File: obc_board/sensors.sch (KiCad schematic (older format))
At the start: 74 parts

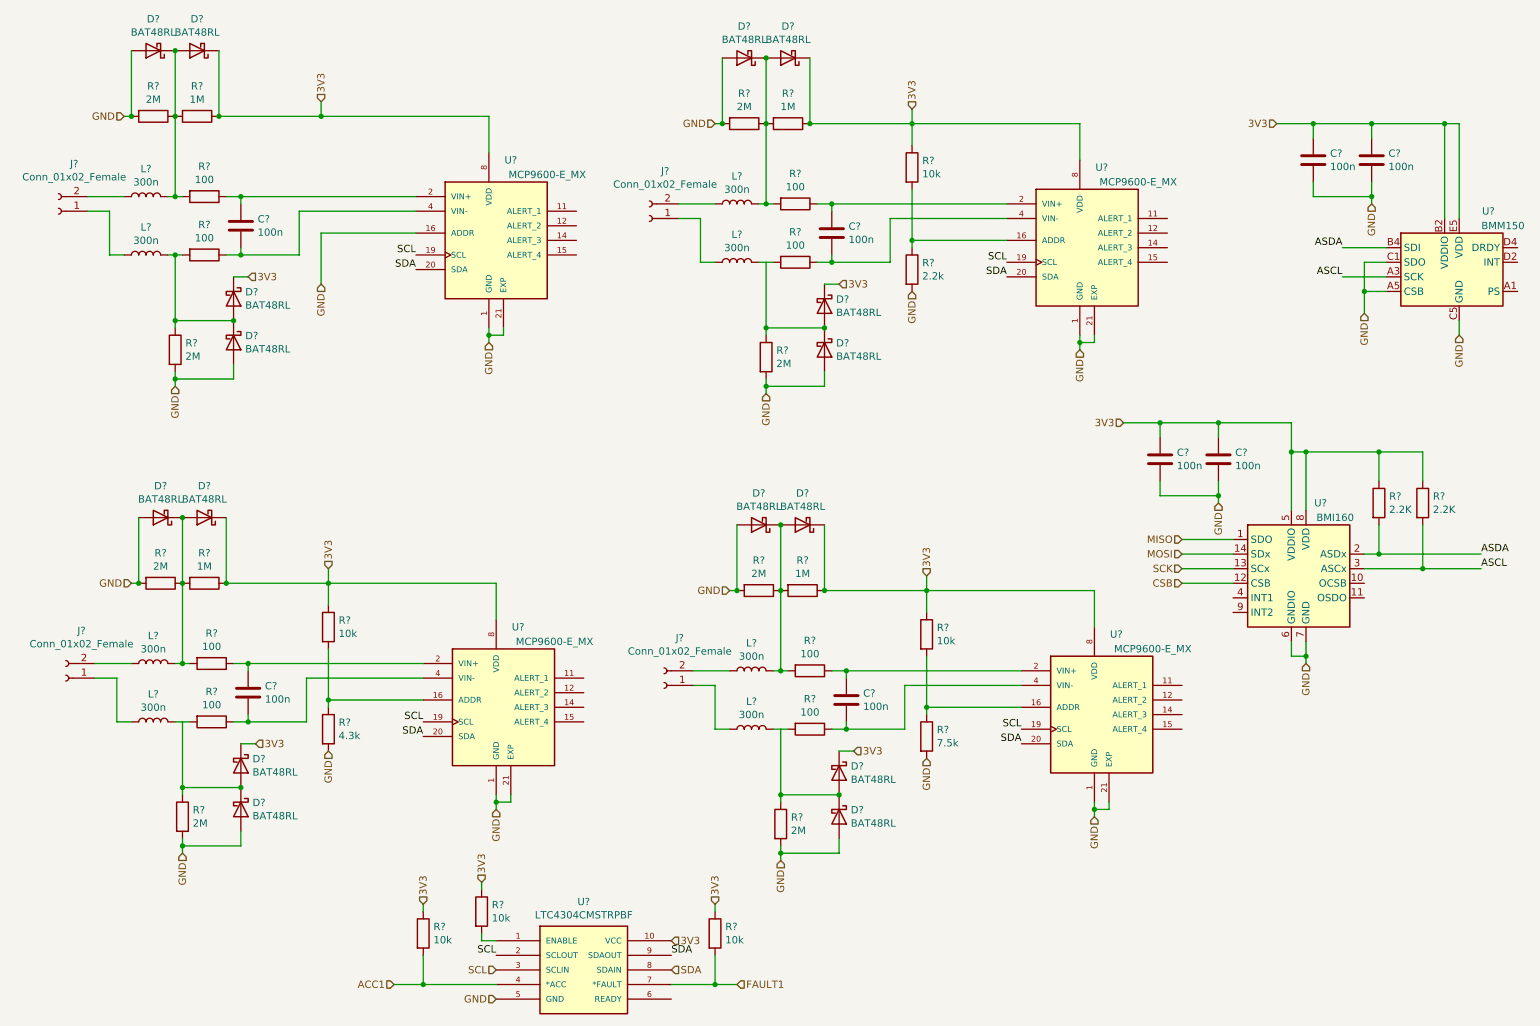
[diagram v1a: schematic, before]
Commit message: updated footprints
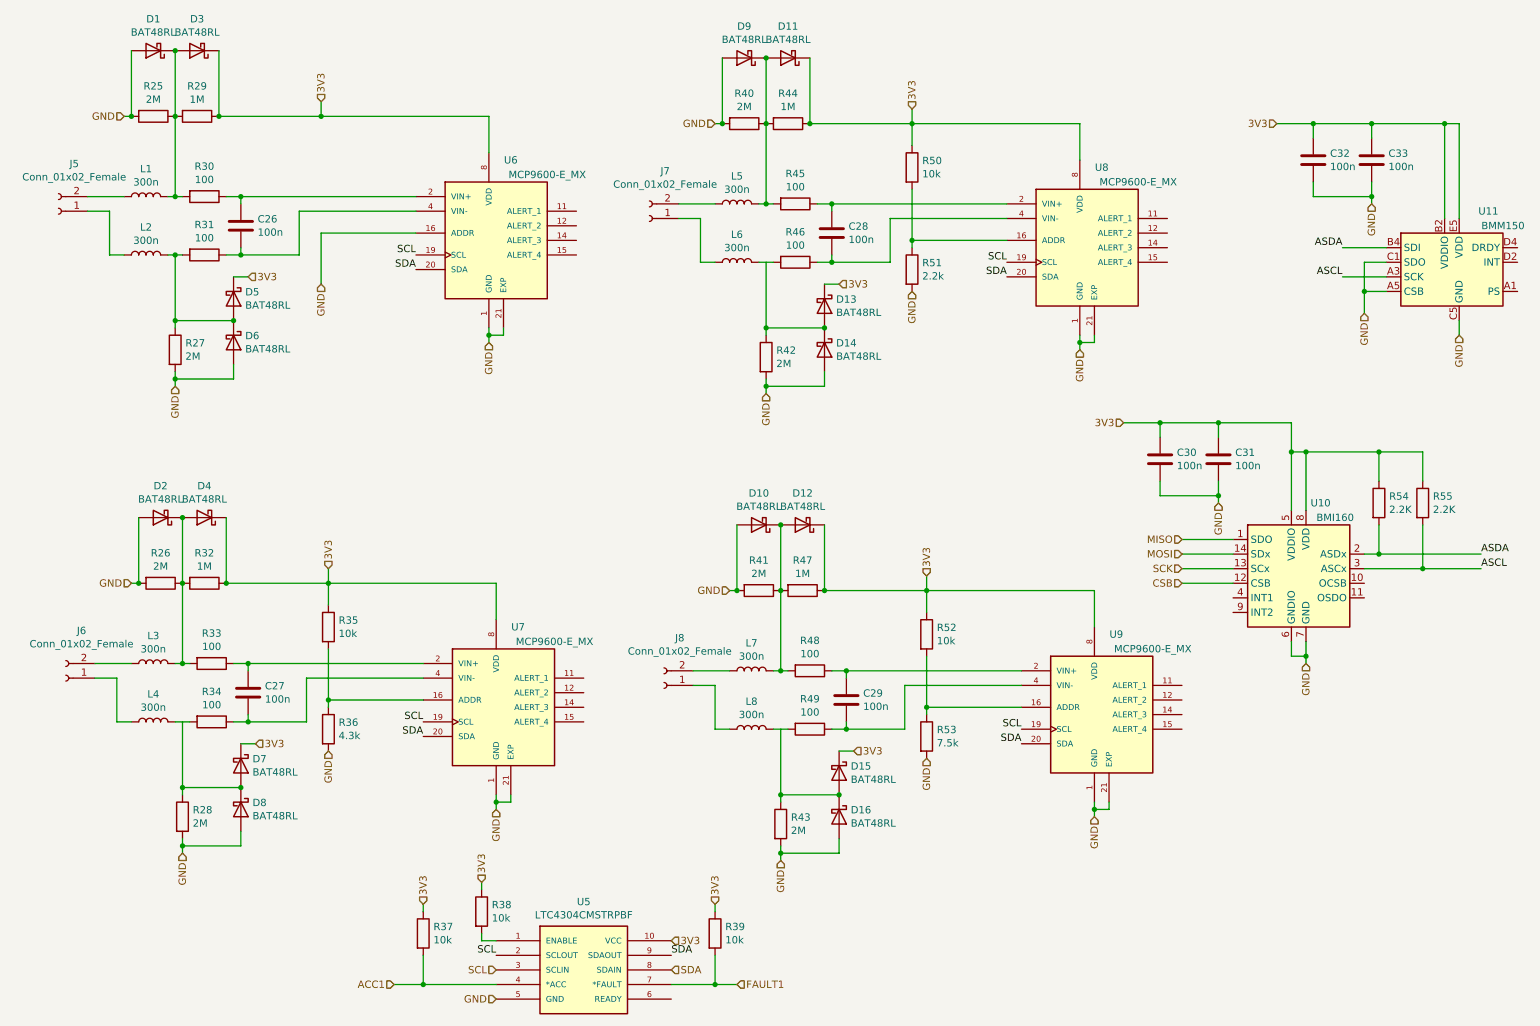
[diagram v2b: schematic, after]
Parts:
- C26, C27, C28, C29, C30, C31, C32, C33: renamed from C?; footprint (none) -> cubesat_obc:CAPC1005X55N; Digikey Part Number (none) -> 490-13342-1-ND
- U10: renamed from U?; Digikey Part Number (none) -> 828-1057-1-ND
- U11: renamed from U?; Digikey Part Number (none) -> 828-1044-1-ND
- U5: renamed from U?; footprint MSOP-10_MS -> Package_SO:MSOP-10_3x3mm_P0.5mm; Digikey Part Number (none) -> LTC4304CMS#PBF-ND
- U6, U7, U8, U9: renamed from U?; footprint QFN65P500X500X100-21N_MCP9600-E/MX -> Package_DFN_QFN:QFN-20-1EP_5x5mm_P0.65mm_EP3.35x3.35mm_ThermalVias; Digikey Part Number (none) -> MCP9600-E/MX-ND
- gave numbers to parts that had none: 59

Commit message: footprints
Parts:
- C26, C27, C28, C29, C30, C31, C32, C33: footprint cubesat_obc:CAPC1005X55N -> Capacitor_SMD:C_0402_1005Metric; Digikey Part Number 490-13342-1-ND -> 490-16433-1-ND
- D1, D10, D11, D12, D13, D14, D15, D16, D2, D3, D4, D5, D6, D7, D8, D9: footprint Diode_THT:D_DO-35_SOD27_P7.62mm_Horizontal -> Diode_SMD:D_MiniMELF; Digikey Part Number (none) -> 497-3274-1-ND
- J5, J6, J7, J8: footprint (none) -> Connector_Molex:Molex_PicoBlade_53398-0271_1x02-1MP_P1.25mm_Vertical; Digikey Part Number (none) -> WM7606CT-ND
- L1, L2, L3, L4, L5, L6, L7, L8: footprint (none) -> Inductor_SMD:L_1210_3225Metric; Digikey Part Number (none) -> 732-7338-2-ND
- R25, R26, R27, R28, R40, R41, R42, R43: footprint (none) -> Resistor_SMD:R_0603_1608Metric; Digikey Part Number (none) -> 311-2.00MHRCT-ND
- R29, R32, R44, R47: footprint (none) -> Resistor_SMD:R_0603_1608Metric; Digikey Part Number (none) -> 11-1.00MHRCT-ND
- R30, R31, R33, R34, R45, R46, R48, R49: footprint (none) -> Resistor_SMD:R_0402_1005Metric; Digikey Part Number (none) -> 311-100LRCT-ND
- R35, R37, R38, R39, R50, R52: footprint (none) -> Resistor_SMD:R_0402_1005Metric; Digikey Part Number (none) -> 311-10.0KLRCT-ND
- R36: footprint (none) -> Resistor_SMD:R_0402_1005Metric; Digikey Part Number (none) -> 311-4.30KLRCT-ND
- R51: footprint (none) -> Resistor_SMD:R_0402_1005Metric; Digikey Part Number (none) -> 311-2.20KLRCT-ND
- R53: footprint (none) -> Resistor_SMD:R_0402_1005Metric; Digikey Part Number (none) -> 311-7.50KLRCT-ND
- R54, R55: value 2.2K -> 2.2k; footprint (none) -> Resistor_SMD:R_0402_1005Metric; Digikey Part Number (none) -> 311-2.20KLRCT-ND
- U5: Field4 Linear Technology -> (none)
- U6, U7, U8, U9: Field4 Microchip -> (none); Field5 1.00mm -> (none); Field6 IPC-7351B -> (none)

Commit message: expose more ios
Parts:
- added R? (x4): 0, symbol Device:R
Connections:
- net 3V3: now also R?.2, R?.2, R?.2, R?.2; no longer D11.1 (K), D12.1 (K), D13.1 (K), D15.1 (K), D3.1 (K), D4.1 (K), D5.1 (K), D7.1 (K), R29.1, R32.1, R35.1, R44.1, R47.1, R50.1, R52.1, U6.8 (VDD), U7.8 (VDD), U8.8 (VDD), U9.8 (VDD)
- new net 3V3_1: D3.1 (K), D5.1 (K), R29.1, R?.1, U6.8 (VDD)
- new net 3V3_2: D11.1 (K), D13.1 (K), R44.1, R50.1, R?.1, U8.8 (VDD)
- new net 3V3_3: D4.1 (K), D7.1 (K), R32.1, R35.1, R?.1, U7.8 (VDD)
- new net 3V3_4: D12.1 (K), D15.1 (K), R47.1, R52.1, R?.1, U9.8 (VDD)
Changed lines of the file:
@@
 $Descr A4 11693 8268
 encoding utf-8
-Sheet 4 5
+Sheet 4 6
 Title ""
 Date ""
@@
 Wire Wire Line
 	1700 3200 1700 3250
-Text HLabel 2200 2500 2    50   Input ~ 0
-3V3
 Wire Wire Line
 	2200 2500 2100 2500
@@
 Wire Wire Line
 	2700 1400 3850 1400
-Text HLabel 2700 1300 1    50   Input ~ 0
-3V3
 Wire Wire Line
 	2700 1300 2700 1400
@@
 Wire Wire Line
 	6750 1450 7900 1450
-Text HLabel 6750 1350 1    50   Input ~ 0
-3V3
 Wire Wire Line
 	6750 1350 6750 1450
@@
 Wire Wire Line
 	2750 4600 3900 4600
-Text HLabel 2750 4500 1    50   Input ~ 0
-3V3
 Wire Wire Line
 	2750 4500 2750 4600
@@
 Wire Wire Line
 	6850 4650 8000 4650
-Text HLabel 6850 4550 1    50   Input ~ 0
-3V3
 Wire Wire Line
 	6850 4550 6850 4650
@@
 Wire Wire Line
 	1750 6400 1750 6450
-Text HLabel 2250 5700 2    50   Input ~ 0
-3V3
 Wire Wire Line
 	2250 5700 2150 5700
@@
 Wire Wire Line
 	5750 3250 5750 3300
-Text HLabel 6250 2550 2    50   Input ~ 0
-3V3
 Wire Wire Line
 	6250 2550 6150 2550
@@
 Wire Wire Line
 	5850 6450 5850 6500
-Text HLabel 6350 5750 2    50   Input ~ 0
-3V3
 Wire Wire Line
 	6350 5750 6250 5750
@@
 	5550 7350 5400 7350
 Connection ~ 5400 7350
+Text Label 6750 1350 1    50   ~ 0
+3V3_2
+Text Label 6250 2550 0    50   ~ 0
+3V3_2
+Text Label 6350 5750 0    50   ~ 0
+3V3_4
+Text Label 6850 4550 1    50   ~ 0
+3V3_4
+Text Label 2250 5700 0    50   ~ 0
+3V3_3
+Text Label 2750 4500 1    50   ~ 0
+3V3_3
+Text Label 2700 1300 1    50   ~ 0
+3V3_1
+Text Label 2200 2500 0    50   ~ 0
+3V3_1
+Text Label 9300 5600 2    50   ~ 0
+3V3_1
+Text Label 9300 5700 2    50   ~ 0
+3V3_2
+Text Label 9300 5800 2    50   ~ 0
+3V3_3
+Text Label 9300 5900 2    50   ~ 0
+3V3_4
+Text HLabel 9300 6400 0    50   Input ~ 0
+3V3
+$Comp
+L Device:R R?
+U 1 1 5F50639E
+P 9550 6150
+F 0 "R?" H 9620 6196 50  0000 L CNN
+F 1 "0" H 9620 6105 50  0000 L CNN
+F 2 "" V 9480 6150 50  0001 C CNN
+F 3 "~" H 9550 6150 50  0001 C CNN
+	1    9550 6150
+	1    0    0    -1
+$EndComp
+$Comp
+L Device:R R?
+U 1 1 5F507ABA
+P 9800 6150
+F 0 "R?" H 9870 6196 50  0000 L CNN
+F 1 "0" H 9870 6105 50  0000 L CNN
+F 2 "" V 9730 6150 50  0001 C CNN
+F 3 "~" H 9800 6150 50  0001 C CNN
+	1    9800 6150
+	1    0    0    -1
+$EndComp
+$Comp
+L Device:R R?
+U 1 1 5F51494E
+P 10050 6150
+F 0 "R?" H 10120 6196 50  0000 L CNN
+F 1 "0" H 10120 6105 50  0000 L CNN
+F 2 "" V 9980 6150 50  0001 C CNN
+F 3 "~" H 10050 6150 50  0001 C CNN
+	1    10050 6150
+	1    0    0    -1
+$EndComp
+$Comp
+L Device:R R?
+U 1 1 5F5215C0
+P 10300 6150
+F 0 "R?" H 10370 6196 50  0000 L CNN
+F 1 "0" H 10370 6105 50  0000 L CNN
+F 2 "" V 10230 6150 50  0001 C CNN
+F 3 "~" H 10300 6150 50  0001 C CNN
+	1    10300 6150
+	1    0    0    -1
+$EndComp
+Wire Wire Line
+	9300 5900 9550 5900
+Wire Wire Line
+	9550 5900 9550 6000
+Wire Wire Line
+	9300 6400 9550 6400
+Wire Wire Line
+	9550 6400 9550 6300
+Wire Wire Line
+	9550 6400 9800 6400
+Wire Wire Line
+	9800 6400 9800 6300
+Connection ~ 9550 6400
+Wire Wire Line
+	9800 6400 10050 6400
+Wire Wire Line
+	10050 6400 10050 6300
+Connection ~ 9800 6400
+Wire Wire Line
+	10050 6400 10300 6400
+Wire Wire Line
+	10300 6400 10300 6300
+Connection ~ 10050 6400
+Wire Wire Line
+	10300 6000 10300 5600
+Wire Wire Line
+	10300 5600 9300 5600
+Wire Wire Line
+	10050 6000 10050 5700
+Wire Wire Line
+	10050 5700 9300 5700
+Wire Wire Line
+	9800 6000 9800 5800
+Wire Wire Line
+	9800 5800 9300 5800
 $EndSCHEMATC

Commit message: footprints
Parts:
- J5, J6, J7, J8: Digikey Part Number WM7606CT-ND -> WM7620CT-ND
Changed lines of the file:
@@
 F 1 "Conn_01x02_Female" H 792 1816 50  0000 C CNN
 F 2 "Connector_Molex:Molex_PicoBlade_53398-0271_1x02-1MP_P1.25mm_Vertical" H 900 2050 50  0001 C CNN
-F 3 "https://www.molex.com/pdm_docs/sd/533980271_sd.pdf~" H 900 2050 50  0001 C CNN
-F 4 "WM7606CT-ND" H 900 2050 50  0001 C CNN "Digikey Part Number"
+F 3 "~" H 900 2050 50  0001 C CNN
+F 4 "WM7620CT-ND" H 900 2050 50  0001 C CNN "Digikey Part Number"
 	1    900  2050
 	-1   0    0    1
@@
 F 1 "Conn_01x02_Female" H 4842 1866 50  0000 C CNN
 F 2 "Connector_Molex:Molex_PicoBlade_53398-0271_1x02-1MP_P1.25mm_Vertical" H 4950 2100 50  0001 C CNN
-F 3 "https://www.molex.com/pdm_docs/sd/533980271_sd.pdf~" H 4950 2100 50  0001 C CNN
-F 4 "WM7606CT-ND" H 4950 2100 50  0001 C CNN "Digikey Part Number"
+F 3 "~" H 4950 2100 50  0001 C CNN
+F 4 "WM7620CT-ND" H 4950 2100 50  0001 C CNN "Digikey Part Number"
 	1    4950 2100
 	-1   0    0    1
@@
 F 1 "Conn_01x02_Female" H 842 5016 50  0000 C CNN
 F 2 "Connector_Molex:Molex_PicoBlade_53398-0271_1x02-1MP_P1.25mm_Vertical" H 950 5250 50  0001 C CNN
-F 3 "https://www.molex.com/pdm_docs/sd/533980271_sd.pdf~" H 950 5250 50  0001 C CNN
-F 4 "WM7606CT-ND" H 950 5250 50  0001 C CNN "Digikey Part Number"
+F 3 "~" H 950 5250 50  0001 C CNN
+F 4 "WM7620CT-ND" H 950 5250 50  0001 C CNN "Digikey Part Number"
 	1    950  5250
 	-1   0    0    1
@@
 F 1 "Conn_01x02_Female" H 4942 5066 50  0000 C CNN
 F 2 "Connector_Molex:Molex_PicoBlade_53398-0271_1x02-1MP_P1.25mm_Vertical" H 5050 5300 50  0001 C CNN
-F 3 "https://www.molex.com/pdm_docs/sd/533980271_sd.pdf~" H 5050 5300 50  0001 C CNN
-F 4 "WM7606CT-ND" H 5050 5300 50  0001 C CNN "Digikey Part Number"
+F 3 "~" H 5050 5300 50  0001 C CNN
+F 4 "WM7620CT-ND" H 5050 5300 50  0001 C CNN "Digikey Part Number"
 	1    5050 5300
 	-1   0    0    1

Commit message: pcb layout
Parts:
- added C36, C37, C38, C39: 100n, Capacitor_SMD:C_0402_1005Metric, symbol Device:C
- added R95, R96, R97, R98: 10k, Resistor_SMD:R_0402_1005Metric, symbol Device:R
- J10: renamed from J5; footprint Connector_Molex:Molex_PicoBlade_53398-0271_1x02-1MP_P1.25mm_Vertical -> Connector_Molex:Molex_PicoBlade_53261-0271_1x02-1MP_P1.25mm_Horizontal
- J11: renamed from J6; footprint Connector_Molex:Molex_PicoBlade_53398-0271_1x02-1MP_P1.25mm_Vertical -> Connector_Molex:Molex_PicoBlade_53261-0271_1x02-1MP_P1.25mm_Horizontal
- J12: renamed from J7; footprint Connector_Molex:Molex_PicoBlade_53398-0271_1x02-1MP_P1.25mm_Vertical -> Connector_Molex:Molex_PicoBlade_53261-0271_1x02-1MP_P1.25mm_Horizontal
- J13: renamed from J8; footprint Connector_Molex:Molex_PicoBlade_53398-0271_1x02-1MP_P1.25mm_Vertical -> Connector_Molex:Molex_PicoBlade_53261-0271_1x02-1MP_P1.25mm_Horizontal
- R51, R52, R54, R56: renamed from R?; footprint (none) -> Resistor_SMD:R_0402_1005Metric; Digikey Part Number (none) -> 311-0.0JRTR-ND
- renumbered R25 to R22, R26 to R23, R27 to R24, R28 to R25, R29 to R26, R30 to R27, R31 to R28, R32 to R29, R33 to R30, R34 to R31, R35 to R32, R36 to R33, R37 to R34, R38 to R35, R39 to R36, R40 to R37, R41 to R38, R42 to R39, R43 to R40, R44 to R41, R45 to R42, R46 to R43, R47 to R44, R48 to R45, R49 to R46, R50 to R47, R51 to R48, R52 to R49, R53 to R50, R54 to R53, U11 to U10, U5 to U4, U6 to U5, U7 to U6, U8 to U7, U9 to U8, U10 to U9
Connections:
- net 3V3: now also R95.1, R96.1, R97.1, R98.1
- net 3V3_1: now also C36.1
- net 3V3_2: now also C38.1
- net 3V3_3: now also C37.1
- net 3V3_4: now also C39.1
- net GND: now also C36.2, C37.2, C38.2, C39.2
- net SCL: now also R95.2, R97.2
- net SDA: now also R96.2, R98.2

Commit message: layout
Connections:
- net at L4.2, R31.2: now also D7.2 (A), D8.1 (K), R25.1
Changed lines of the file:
@@
 	1700 2350 1750 2350
 Connection ~ 1700 2800
-Wire Wire Line
-	1700 5550 1800 5550
 $Comp
 L Device:R R25
@@
 Wire Wire Line
 	2250 5700 2150 5700
-Wire Wire Line
-	1750 5550 1750 6000
-Connection ~ 1750 6000
 Wire Wire Line
 	5700 2400 5800 2400
@@
 Text HLabel 2050 7450 0    50   Input ~ 0
 SDA
+Wire Wire Line
+	1700 5550 1750 5550
+Wire Wire Line
+	1750 5550 1750 6000
+Connection ~ 1750 5550
+Wire Wire Line
+	1750 5550 1800 5550
+Connection ~ 1750 6000
 $EndSCHEMATC

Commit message: layout
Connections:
- net SCL: no longer R97.2, U4.3 (SCLIN)
- net SDA: no longer R98.2, U4.8 (SDAIN)
- new net SCL1: R97.2, U4.3 (SCLIN)
- new net SDA1: R98.2, U4.8 (SDAIN)
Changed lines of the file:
@@
 $Descr A4 11693 8268
 encoding utf-8
-Sheet 4 7
+Sheet 4 8
 Title ""
 Date ""
@@
 	1    3950 2300
 	1    0    0    -1
-$EndComp
-$Comp
-L Connector:Conn_01x02_Female J10
-U 1 1 5F37DDB8
-P 900 2050
-F 0 "J10" H 792 1725 50  0000 C CNN
-F 1 "Conn_01x02_Female" H 792 1816 50  0000 C CNN
-F 2 "Connector_Molex:Molex_PicoBlade_53261-0271_1x02-1MP_P1.25mm_Horizontal" H 900 2050 50  0001 C CNN
-F 3 "https://www.molex.com/pdm_docs/sd/532610271_sd.pdf" H 900 2050 50  0001 C CNN
-F 4 "WM7620CT-ND" H 900 2050 50  0001 C CNN "Digikey Part Number"
-	1    900  2050
-	-1   0    0    1
 $EndComp
 $Comp
@@
 SDA
 Text HLabel 3900 7250 0    50   Input ~ 0
-SCL
-Text HLabel 5100 7250 2    50   Input ~ 0
-SDA
+SCL1
 $Comp
 L Device:R R35
@@
 	2050 7450 2800 7450
 Text HLabel 2050 7350 0    50   Input ~ 0
-SCL
+SCL1
 Text HLabel 2050 7450 0    50   Input ~ 0
-SDA
+SDA1
 Wire Wire Line
 	1700 5550 1750 5550
@@
 	1750 5550 1800 5550
 Connection ~ 1750 6000
+$Comp
+L Connector:Conn_01x02_Female J10
+U 1 1 5F37DDB8
+P 900 2050
+F 0 "J10" H 792 1725 50  0000 C CNN
+F 1 "Conn_01x02_Female" H 792 1816 50  0000 C CNN
+F 2 "Connector_Molex:Molex_PicoBlade_53261-0271_1x02-1MP_P1.25mm_Horizontal" H 900 2050 50  0001 C CNN
+F 3 "https://www.molex.com/pdm_docs/sd/532610271_sd.pdf" H 900 2050 50  0001 C CNN
+F 4 "WM7620CT-ND" H 900 2050 50  0001 C CNN "Digikey Part Number"
+	1    900  2050
+	-1   0    0    1
+$EndComp
+Text HLabel 5100 7250 2    50   Input ~ 0
+SDA1
 $EndSCHEMATC
